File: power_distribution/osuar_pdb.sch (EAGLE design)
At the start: 27 parts, among them J1 M02, J2 M02, J3 M02, J4 M02, J5 M02, J6 M02, J7 M02, J8 M02

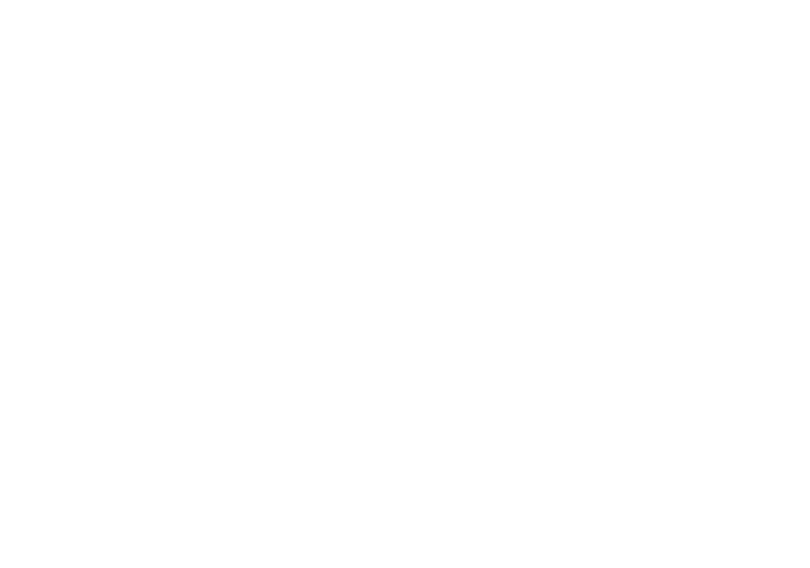
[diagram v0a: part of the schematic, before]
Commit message: Add extra Vin connector to pdb schematic
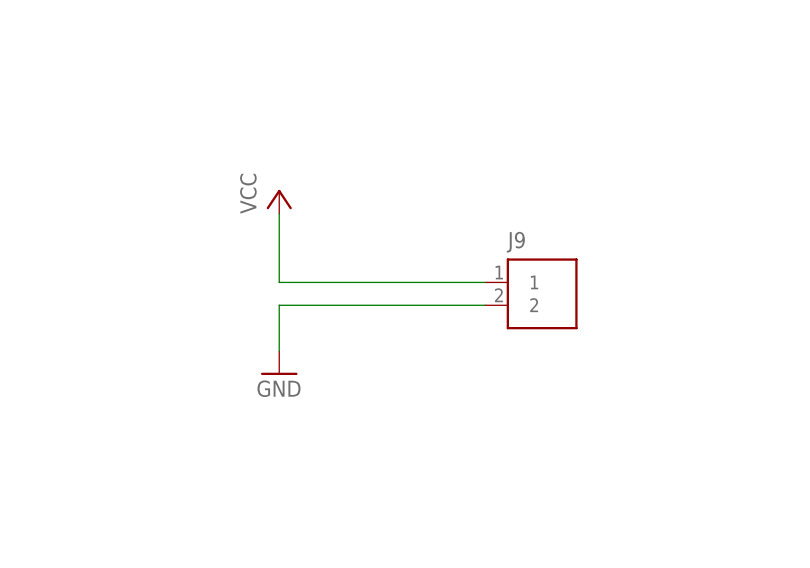
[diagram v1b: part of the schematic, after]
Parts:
- added J9: M02, OSURC_Connectors:M02
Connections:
- net GND: now also J9.2
- net VCC: now also J9.1
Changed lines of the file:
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@@
 <?xml version="1.0" encoding="utf-8"?>
 <!DOCTYPE eagle SYSTEM "eagle.dtd">
-<eagle version="7.1.0">
+<eagle version="6.5.0">
 <drawing>
 <settings>
@@
 <part name="GND15" library="supply1" deviceset="GND" device=""/>
 <part name="P+5" library="supply1" deviceset="VCC" device=""/>
+<part name="J9" library="OSURC_Connectors" deviceset="M02" device=""/>
+<part name="GND3" library="supply1" deviceset="GND" device=""/>
+<part name="P+6" library="supply1" deviceset="VCC" device=""/>
 </parts>
 <sheets>
@@
 <instance part="GND15" gate="1" x="40.64" y="-342.9"/>
 <instance part="P+5" gate="VCC" x="40.64" y="-325.12"/>
+<instance part="J9" gate="G$1" x="68.58" y="-289.56"/>
+<instance part="GND3" gate="1" x="40.64" y="-297.18"/>
+<instance part="P+6" gate="VCC" x="40.64" y="-276.86"/>
 </instances>
 <busses>
@@
 <wire x1="144.78" y1="-243.84" x2="144.78" y2="-246.38" width="0.1524" layer="91"/>
 </segment>
+<segment>
+<pinref part="GND3" gate="1" pin="GND"/>
+<pinref part="J9" gate="G$1" pin="2"/>
+<wire x1="40.64" y1="-294.64" x2="40.64" y2="-289.56" width="0.1524" layer="91"/>
+<wire x1="40.64" y1="-289.56" x2="63.5" y2="-289.56" width="0.1524" layer="91"/>
+</segment>
 </net>
 <net name="N$3" class="0">
@@
 <junction x="5.08" y="-116.84"/>
 </segment>
-</net>
+<segment>
+<pinref part="J9" gate="G$1" pin="1"/>
+<pinref part="P+6" gate="VCC" pin="VCC"/>
+<wire x1="63.5" y1="-287.02" x2="40.64" y2="-287.02" width="0.1524" layer="91"/>
+<wire x1="40.64" y1="-287.02" x2="40.64" y2="-279.4" width="0.1524" layer="91"/>
+</segment>
+</net>
